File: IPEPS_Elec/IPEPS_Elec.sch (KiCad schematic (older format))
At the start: 26 parts

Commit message: secure AND unused inputs
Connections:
- wire segments 96 -> 100
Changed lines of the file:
@@
 	1    0    0    -1
 $EndComp
+$Comp
+L power:VCC #PWR?
+U 1 1 619B6EE2
+P 3735 4095
+F 0 "#PWR?" H 3735 3945 50  0001 C CNN
+F 1 "VCC" H 3750 4268 50  0000 C CNN
+F 2 "" H 3735 4095 50  0001 C CNN
+F 3 "" H 3735 4095 50  0001 C CNN
+	1    3735 4095
+	1    0    0    -1
+$EndComp
+$Comp
+L power:VCC #PWR?
+U 1 1 619B7C4D
+P 7340 1980
+F 0 "#PWR?" H 7340 1830 50  0001 C CNN
+F 1 "VCC" H 7355 2153 50  0000 C CNN
+F 2 "" H 7340 1980 50  0001 C CNN
+F 3 "" H 7340 1980 50  0001 C CNN
+	1    7340 1980
+	1    0    0    -1
+$EndComp
+Wire Wire Line
+	3735 4095 3735 4400
+Wire Wire Line
+	3735 4400 3860 4400
+Wire Wire Line
+	7340 1980 7340 2300
+Wire Wire Line
+	7340 2300 7440 2300
 $EndSCHEMATC

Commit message: wire the leds + add comments
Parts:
- removed D? (x3): LED, symbol Device:LED
- removed Q? (x3): BC547, Package_TO_SOT_THT:TO-92_Inline, symbol Transistor_BJT:BC547
- removed R? (x2): R_Small, symbol Device:R_Small
- added D?: T, symbol Device:LED
- added D?: L, symbol Device:LED
- added D?: RJ, symbol Device:LED
- added Q? (x3): BC547, Package_TO_SOT_THT:TO-92_Inline, symbol Transistor_BJT:BC547
- added R? (x3): 220R, symbol Device:R_Small
- added R? (x3): 47k, symbol Device:R_Small
- D?: value LED -> C; Colour (none) -> Green
- R?: value R_Small -> 220R
- R?: value R_Small -> 47k
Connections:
- net labels added: Out_C, Out_L, Out_RJ, Out_T
- wire segments 100 -> 108
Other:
- moved on the sheet: D?, Q?, R?

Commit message: simplify the XNOR
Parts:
- removed C?: 10uF, symbol Device:C_Small
- removed U?: SN74HC86N, digikey-footprints:DIP-14_W3mm, symbol IPEPS_Elec:SN74HC86N
- added U?: CD74HC7266E, Package_DIP:DIP-14_W7.62mm, symbol IPEPS_Elec:CD74HC7266E
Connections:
- wire segments 108 -> 99
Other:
- moved on the sheet: BAT?, Q?
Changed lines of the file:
@@
 L dk_Battery-Holders-Clips-Contacts:BS-7 BAT?
 U 1 1 61827D44
-P 1075 1625
-F 0 "BAT?" H 725 1700 60  0000 L CNN
-F 1 "BS-7" H 700 1600 60  0000 L CNN
-F 2 "digikey-footprints:Battery_Holder_Coin_2032_BS-7" H 1275 1825 60  0001 L CNN
-F 3 "http://www.memoryprotectiondevices.com/datasheets/BS-7-datasheet.pdf" V 1275 1925 60  0001 L CNN
-F 4 "BS-7-ND" H 1275 2025 60  0001 L CNN "Digi-Key_PN"
-F 5 "BS-7" H 1275 2125 60  0001 L CNN "MPN"
-F 6 "Battery Products" H 1275 2225 60  0001 L CNN "Category"
-F 7 "Battery Holders, Clips, Contacts" H 1275 2325 60  0001 L CNN "Family"
-F 8 "http://www.memoryprotectiondevices.com/datasheets/BS-7-datasheet.pdf" H 1275 2425 60  0001 L CNN "DK_Datasheet_Link"
-F 9 "/product-detail/en/mpd-memory-protection-devices/BS-7/BS-7-ND/389447" H 1275 2525 60  0001 L CNN "DK_Detail_Page"
-F 10 "BATTERY HOLDER COIN 20MM PC PIN" H 1275 2625 60  0001 L CNN "Description"
-F 11 "MPD (Memory Protection Devices)" H 1275 2725 60  0001 L CNN "Manufacturer"
-F 12 "Active" H 1275 2825 60  0001 L CNN "Status"
-	1    1075 1625
-	1    0    0    -1
-$EndComp
-Wire Wire Line
-	1750 1375 1075 1375
-Wire Wire Line
-	1075 1375 1075 1425
-Wire Wire Line
-	1075 1825 1950 1825
-Wire Wire Line
-	1950 1825 1950 1675
+P 945 1170
+F 0 "BAT?" H 595 1245 60  0000 L CNN
+F 1 "BS-7" H 570 1145 60  0000 L CNN
+F 2 "digikey-footprints:Battery_Holder_Coin_2032_BS-7" H 1145 1370 60  0001 L CNN
+F 3 "http://www.memoryprotectiondevices.com/datasheets/BS-7-datasheet.pdf" V 1145 1470 60  0001 L CNN
+F 4 "BS-7-ND" H 1145 1570 60  0001 L CNN "Digi-Key_PN"
+F 5 "BS-7" H 1145 1670 60  0001 L CNN "MPN"
+F 6 "Battery Products" H 1145 1770 60  0001 L CNN "Category"
+F 7 "Battery Holders, Clips, Contacts" H 1145 1870 60  0001 L CNN "Family"
+F 8 "http://www.memoryprotectiondevices.com/datasheets/BS-7-datasheet.pdf" H 1145 1970 60  0001 L CNN "DK_Datasheet_Link"
+F 9 "/product-detail/en/mpd-memory-protection-devices/BS-7/BS-7-ND/389447" H 1145 2070 60  0001 L CNN "DK_Detail_Page"
+F 10 "BATTERY HOLDER COIN 20MM PC PIN" H 1145 2170 60  0001 L CNN "Description"
+F 11 "MPD (Memory Protection Devices)" H 1145 2270 60  0001 L CNN "Manufacturer"
+F 12 "Active" H 1145 2370 60  0001 L CNN "Status"
+	1    945  1170
+	1    0    0    -1
+$EndComp
+Wire Wire Line
+	1620 920  945  920
+Wire Wire Line
+	945  920  945  970
+Wire Wire Line
+	945  1370 1820 1370
+Wire Wire Line
+	1820 1370 1820 1220
 $Comp
 L power:GND #PWR?
 U 1 1 61830670
-P 1075 1875
-F 0 "#PWR?" H 1075 1625 50  0001 C CNN
-F 1 "GND" H 1080 1702 50  0000 C CNN
-F 2 "" H 1075 1875 50  0001 C CNN
-F 3 "" H 1075 1875 50  0001 C CNN
-	1    1075 1875
-	1    0    0    -1
-$EndComp
-Wire Wire Line
-	1075 1825 1075 1875
-Connection ~ 1075 1825
+P 945 1420
+F 0 "#PWR?" H 945 1170 50  0001 C CNN
+F 1 "GND" H 950 1247 50  0000 C CNN
+F 2 "" H 945 1420 50  0001 C CNN
+F 3 "" H 945 1420 50  0001 C CNN
+	1    945  1420
+	1    0    0    -1
+$EndComp
+Wire Wire Line
+	945  1370 945  1420
+Connection ~ 945  1370
 $Comp
 L IPEPS_Elec:SN74HC11N U?
@@
 L Transistor_FET:AO3401A Q?
 U 1 1 61893D18
-P 1950 1475
-F 0 "Q?" V 2292 1475 50  0000 C CNN
-F 1 "AO3401A" V 2201 1475 50  0000 C CNN
-F 2 "Package_TO_SOT_SMD:SOT-23" H 2150 1400 50  0001 L CIN
-F 3 "http://www.aosmd.com/pdfs/datasheet/AO3401A.pdf" H 1950 1475 50  0001 L CNN
-	1    1950 1475
+P 1820 1020
+F 0 "Q?" V 2162 1020 50  0000 C CNN
+F 1 "AO3401A" V 2071 1020 50  0000 C CNN
+F 2 "Package_TO_SOT_SMD:SOT-23" H 2020 945 50  0001 L CIN
+F 3 "http://www.aosmd.com/pdfs/datasheet/AO3401A.pdf" H 1820 1020 50  0001 L CNN
+	1    1820 1020
 	0    -1   -1   0
 $EndComp
@@
 L power:VCC #PWR?
 U 1 1 61896917
-P 2300 1300
-F 0 "#PWR?" H 2300 1150 50  0001 C CNN
-F 1 "VCC" H 2315 1473 50  0000 C CNN
-F 2 "" H 2300 1300 50  0001 C CNN
-F 3 "" H 2300 1300 50  0001 C CNN
-	1    2300 1300
+P 2170 845
+F 0 "#PWR?" H 2170 695 50  0001 C CNN
+F 1 "VCC" H 2185 1018 50  0000 C CNN
+F 2 "" H 2170 845 50  0001 C CNN
+F 3 "" H 2170 845 50  0001 C CNN
+	1    2170 845
 	1    0    0    -1
 $EndComp
@@
 $EndComp
 Wire Wire Line
-	2150 1375 2300 1375
-Wire Wire Line
-	2300 1375 2300 1300
+	2020 920  2170 920
+Wire Wire Line
+	2170 920  2170 845
 $Comp
 L power:VCC #PWR?
@@
 	1    0    0    -1
 $EndComp
-Connection ~ 7100 3560
-Wire Wire Line
-	7100 3560 7100 3715
-Wire Wire Line
-	6600 3560 7100 3560
-Wire Wire Line
-	7100 3560 7100 3485
-$Comp
-L power:VCC #PWR?
-U 1 1 618FABB9
-P 7100 3485
-F 0 "#PWR?" H 7100 3335 50  0001 C CNN
-F 1 "VCC" H 7115 3658 50  0000 C CNN
-F 2 "" H 7100 3485 50  0001 C CNN
-F 3 "" H 7100 3485 50  0001 C CNN
-	1    7100 3485
-	1    0    0    -1
-$EndComp
-$Comp
-L Device:C_Small C?
-U 1 1 618F83E8
-P 6600 3660
-F 0 "C?" H 6475 3760 50  0000 L CNN
-F 1 "10uF" H 6375 3585 50  0000 L CNN
-F 2 "" H 6600 3660 50  0001 C CNN
-F 3 "~" H 6600 3660 50  0001 C CNN
-	1    6600 3660
-	1    0    0    -1
-$EndComp
-$Comp
-L power:GND #PWR?
-U 1 1 618F8054
-P 6600 3760
-F 0 "#PWR?" H 6600 3510 50  0001 C CNN
-F 1 "GND" H 6605 3587 50  0001 C CNN
-F 2 "" H 6600 3760 50  0001 C CNN
-F 3 "" H 6600 3760 50  0001 C CNN
-	1    6600 3760
-	1    0    0    -1
-$EndComp
-$Comp
-L IPEPS_Elec:SN74HC86N U?
-U 1 1 618F3369
-P 7100 5035
-F 0 "U?" H 6825 6310 50  0000 C CNN
-F 1 "SN74HC86N" H 7475 3810 50  0000 C CNN
-F 2 "digikey-footprints:DIP-14_W3mm" H 7830 6325 50  0001 C CNN
-F 3 "https://www.ti.com/lit/ds/symlink/sn74hc86.pdf?ts=1635939524941&ref_url=https%253A%252F%252Fwww.google.com%252F" H 7100 5305 50  0001 C CNN
-	1    7100 5035
-	1    0    0    -1
-$EndComp
 Wire Wire Line
 	2545 4200 2545 5415
@@
 Wire Wire Line
 	6460 5565 6460 4335
-Wire Wire Line
-	6460 4335 6660 4335
 Connection ~ 2400 4300
-Wire Wire Line
-	3815 1565 3655 1565
-Wire Wire Line
-	3655 1565 3655 2425
-Wire Wire Line
-	3655 2425 6515 2425
-Wire Wire Line
-	6515 2425 6515 3250
-Wire Wire Line
-	6515 3250 7530 3250
-Wire Wire Line
-	7530 3250 7530 4235
-Wire Wire Line
-	4415 1565 5700 1565
-Wire Wire Line
-	5700 1565 5700 2100
-Wire Wire Line
-	5700 2100 7440 2100
 Wire Wire Line
 	7225 2265 7225 2200
@@
 Wire Wire Line
 	10215 6050 10250 6050
+$Comp
+L IPEPS_Elec:CD74HC7266E U?
+U 1 1 6192A273
+P 6970 4235
+F 0 "U?" H 6970 4560 50  0000 C CNN
+F 1 "CD74HC7266E" H 6970 4469 50  0000 C CNN
+F 2 "Package_DIP:DIP-14_W7.62mm" H 6960 3935 50  0001 C CNN
+F 3 "https://www.ti.com/lit/ds/symlink/cd74hc7266.pdf" H 6970 4235 50  0001 C CNN
+	1    6970 4235
+	1    0    0    -1
+$EndComp
+Wire Wire Line
+	6460 4335 6670 4335
+Wire Wire Line
+	7270 4240 7270 4235
+Wire Wire Line
+	7270 2100 7440 2100
+Connection ~ 7270 4235
+Wire Wire Line
+	7270 4235 7270 2100
 $EndSCHEMATC

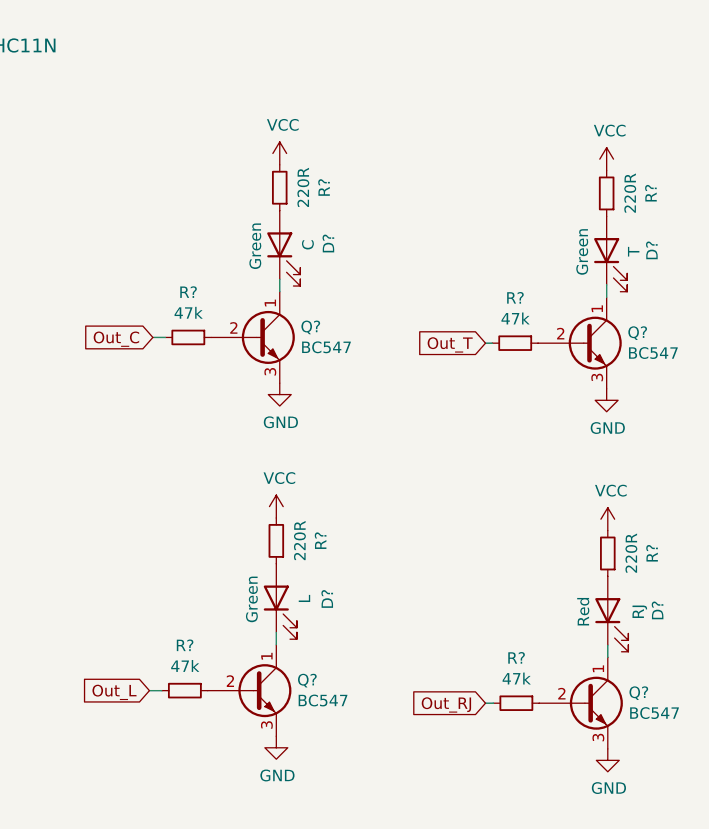
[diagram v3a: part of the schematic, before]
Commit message: change resistor values for 3V
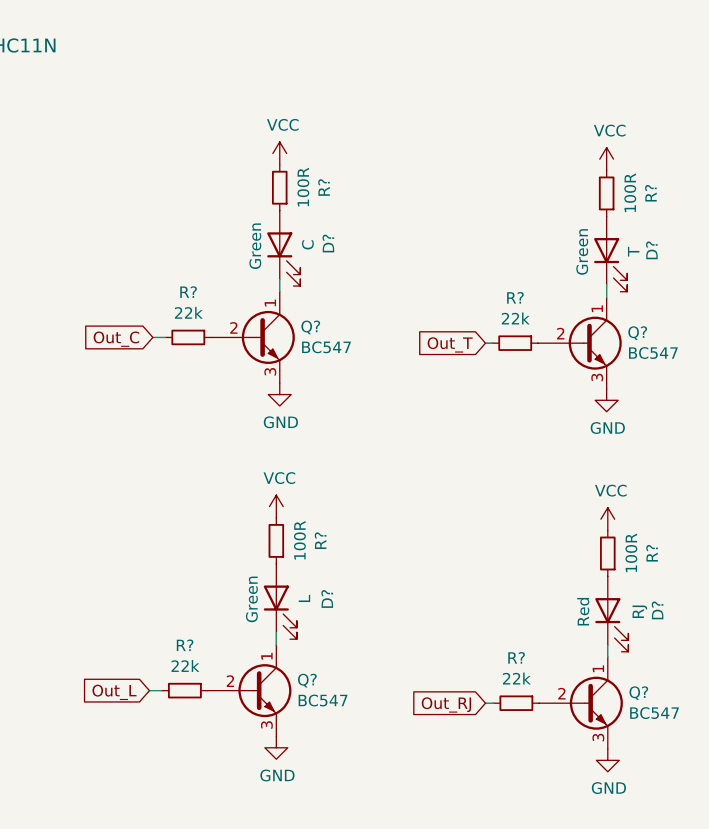
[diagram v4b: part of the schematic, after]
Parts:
- R? (x4): value 220R -> 100R
- R? (x4): value 47k -> 22k

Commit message: reorganise components
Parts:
- added R? (x4): 10k, symbol Device:R_Small
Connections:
- net GND: now also R?.1, R?.1, R?.1, R?.1
- net Out_C: now also U?.12 (1Y)
- net Out_L: now also U?.12 (1Y)
- net Out_RJ: now also U?.6 (2Y)
- net Out_T: now also U?.6 (2Y)
- net VCC: now also U?.3 (2A), U?.9 (3A); no longer U?.11 (3C), U?.5 (2C)
- net at U?.1 (1A): now also SW?.2, U?.1 (1A), U?.10 (3B), U?.2, R?.2; no longer U?.6 (3Y)
- net at U?.11 (3C): now also SW?.2, U?.1, U?.3 (2A), U?.3 (2A)
- net IN_J: now reaches SW?.2, U?.13 (1C), U?.13 (1C)
- net IN_J: now also U?.4 (2B), U?.5 (2C), R?.2; no longer U?.4 (2B), U?.5 (2C)
- net at U?.2 (1B): now also U?.4 (2Y); no longer SW?.2
- net at U?.3: now also U?.5 (2C); no longer U?.3 (2A)
- net C+T: now reaches U?.8 (3Y)
- net C+T: now also U?.5 (3A)
- net at U?.2 (1Y): now also U?.4 (2B); no longer U?.2 (1B)
- net at U?.8 (3Y): no longer U?.5 (3A)
- new net: R?.2, SW?.2, U?.1 (1A)
- new net: U?.2 (1B), U?.6 (3Y)
- now unconnected: U?.10 (3B), U?.9 (3A)
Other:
- moved on the sheet: BAT?, C?, D?, Q?, R?, SW?, U?, U?A

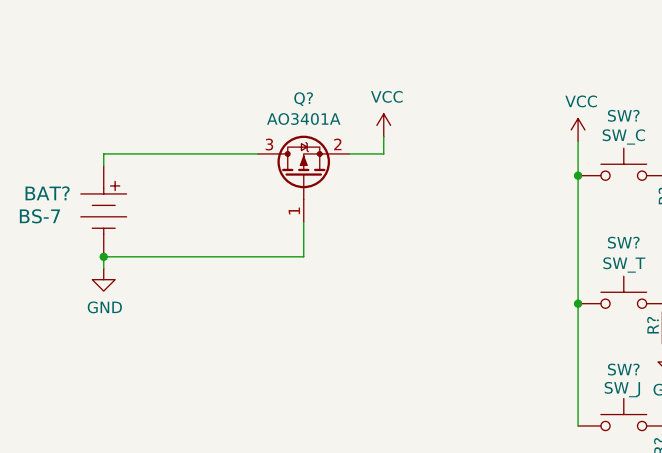
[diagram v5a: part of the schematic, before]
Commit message: add main switch
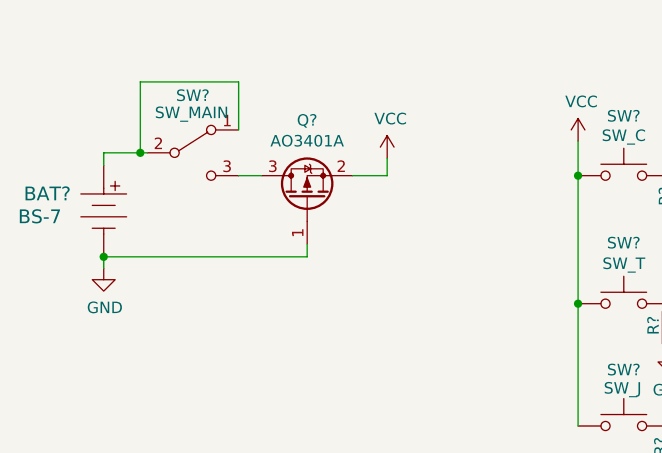
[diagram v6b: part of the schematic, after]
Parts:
- added SW?: SW_MAIN, symbol Switch:SW_SPDT
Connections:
- net at BAT?.Pos: now also SW?.1 (A), SW?.2 (B); no longer Q?.3 (D)
- new net: Q?.3 (D), SW?.3 (C)
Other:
- moved on the sheet: Q?
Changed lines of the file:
@@
 	1    0    0    -1
 $EndComp
-Wire Wire Line
-	1735 1205 1060 1205
-Wire Wire Line
-	1060 1205 1060 1255
-Wire Wire Line
-	1060 1655 1935 1655
-Wire Wire Line
-	1935 1655 1935 1505
 $Comp
 L power:GND #PWR?
@@
 L Transistor_FET:AO3401A Q?
 U 1 1 61893D18
-P 1935 1305
-F 0 "Q?" V 2277 1305 50  0000 C CNN
-F 1 "AO3401A" V 2186 1305 50  0000 C CNN
-F 2 "Package_TO_SOT_SMD:SOT-23" H 2135 1230 50  0001 L CIN
-F 3 "http://www.aosmd.com/pdfs/datasheet/AO3401A.pdf" H 1935 1305 50  0001 L CNN
-	1    1935 1305
+P 1950 1400
+F 0 "Q?" V 2292 1400 50  0000 C CNN
+F 1 "AO3401A" V 2201 1400 50  0000 C CNN
+F 2 "Package_TO_SOT_SMD:SOT-23" H 2150 1325 50  0001 L CIN
+F 3 "http://www.aosmd.com/pdfs/datasheet/AO3401A.pdf" H 1950 1400 50  0001 L CNN
+	1    1950 1400
 	0    -1   -1   0
 $EndComp
@@
 L power:VCC #PWR?
 U 1 1 61896917
-P 2285 1130
-F 0 "#PWR?" H 2285 980 50  0001 C CNN
-F 1 "VCC" H 2300 1303 50  0000 C CNN
-F 2 "" H 2285 1130 50  0001 C CNN
-F 3 "" H 2285 1130 50  0001 C CNN
-	1    2285 1130
+P 2300 1225
+F 0 "#PWR?" H 2300 1075 50  0001 C CNN
+F 1 "VCC" H 2315 1398 50  0000 C CNN
+F 2 "" H 2300 1225 50  0001 C CNN
+F 3 "" H 2300 1225 50  0001 C CNN
+	1    2300 1225
 	1    0    0    -1
 $EndComp
@@
 $EndComp
 Wire Wire Line
-	2135 1205 2285 1205
-Wire Wire Line
-	2285 1205 2285 1130
+	2150 1300 2300 1300
+Wire Wire Line
+	2300 1300 2300 1225
 $Comp
 L power:VCC #PWR?
@@
 Wire Wire Line
 	5220 5650 6230 5650
+$Comp
+L Switch:SW_SPDT SW?
+U 1 1 61B3D302
+P 1450 1200
+F 0 "SW?" H 1450 1450 50  0000 C CNN
+F 1 "SW_MAIN" H 1445 1375 50  0000 C CNN
+F 2 "" H 1450 1200 50  0001 C CNN
+F 3 "~" H 1450 1200 50  0001 C CNN
+	1    1450 1200
+	1    0    0    -1
+$EndComp
+Wire Wire Line
+	1950 1655 1950 1600
+Wire Wire Line
+	1060 1655 1950 1655
+Wire Wire Line
+	1650 1300 1750 1300
+Wire Wire Line
+	1060 1200 1220 1200
+Wire Wire Line
+	1060 1200 1060 1255
+Connection ~ 1220 1200
+Wire Wire Line
+	1220 1200 1250 1200
+Wire Wire Line
+	1650 890  1220 890
+Wire Wire Line
+	1650 890  1650 1100
+Wire Wire Line
+	1220 890  1220 1200
 $EndSCHEMATC

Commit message: add main decoupler
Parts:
- added C?: 10uF, symbol Device:CP1_Small
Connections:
- net GND: now also C?.2
- net VCC: now also C?.1
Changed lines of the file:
@@
 L power:VCC #PWR?
 U 1 1 61896917
-P 2300 1225
-F 0 "#PWR?" H 2300 1075 50  0001 C CNN
-F 1 "VCC" H 2315 1398 50  0000 C CNN
-F 2 "" H 2300 1225 50  0001 C CNN
-F 3 "" H 2300 1225 50  0001 C CNN
-	1    2300 1225
+P 2415 1230
+F 0 "#PWR?" H 2415 1080 50  0001 C CNN
+F 1 "VCC" H 2430 1403 50  0000 C CNN
+F 2 "" H 2415 1230 50  0001 C CNN
+F 3 "" H 2415 1230 50  0001 C CNN
+	1    2415 1230
 	1    0    0    -1
 $EndComp
@@
 	1    0    0    -1
 $EndComp
-Wire Wire Line
-	2150 1300 2300 1300
-Wire Wire Line
-	2300 1300 2300 1225
 $Comp
 L power:VCC #PWR?
@@
 Wire Wire Line
 	1220 890  1220 1200
+Wire Wire Line
+	2415 1300 2415 1230
+Wire Wire Line
+	2150 1300 2245 1300
+$Comp
+L Device:CP1_Small C?
+U 1 1 61B576AA
+P 2245 1440
+F 0 "C?" H 2336 1486 50  0000 L CNN
+F 1 "10uF" H 2336 1395 50  0000 L CNN
+F 2 "" H 2245 1440 50  0001 C CNN
+F 3 "~" H 2245 1440 50  0001 C CNN
+	1    2245 1440
+	1    0    0    -1
+$EndComp
+Wire Wire Line
+	2245 1340 2245 1300
+Connection ~ 2245 1300
+Wire Wire Line
+	2245 1300 2415 1300
+$Comp
+L power:GND #PWR?
+U 1 1 61B5BC87
+P 2245 1540
+F 0 "#PWR?" H 2245 1290 50  0001 C CNN
+F 1 "GND" H 2250 1367 50  0000 C CNN
+F 2 "" H 2245 1540 50  0001 C CNN
+F 3 "" H 2245 1540 50  0001 C CNN
+	1    2245 1540
+	1    0    0    -1
+$EndComp
 $EndSCHEMATC

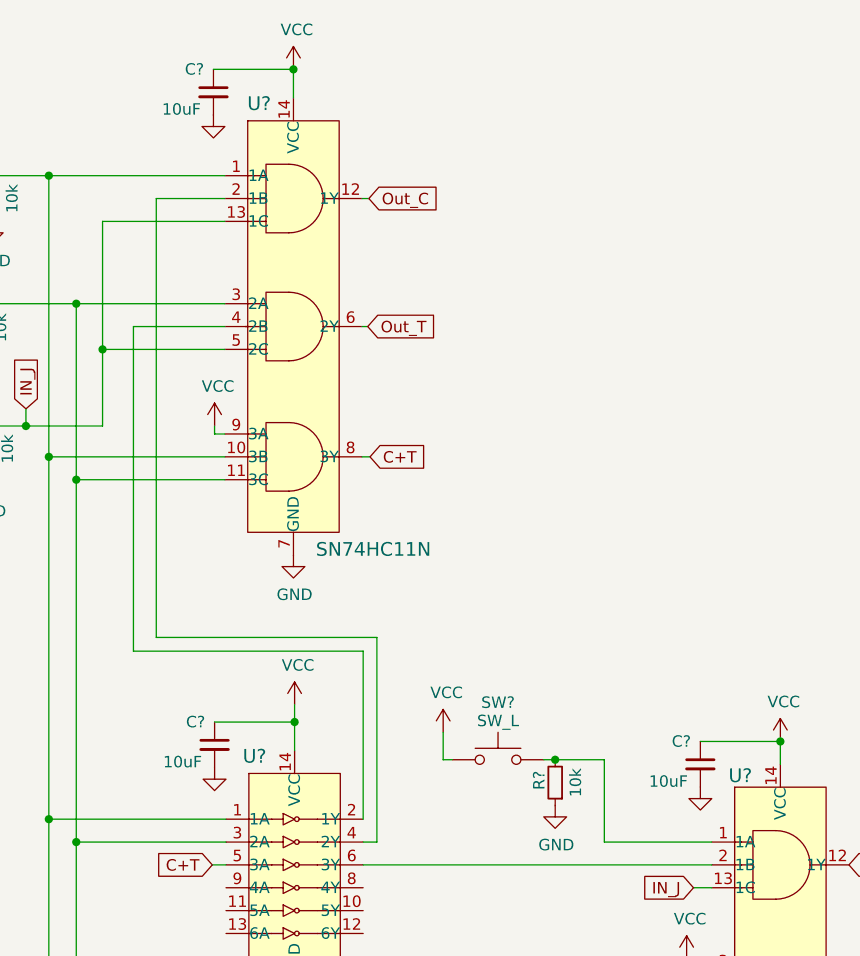
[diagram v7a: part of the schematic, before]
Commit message: change decouplers values
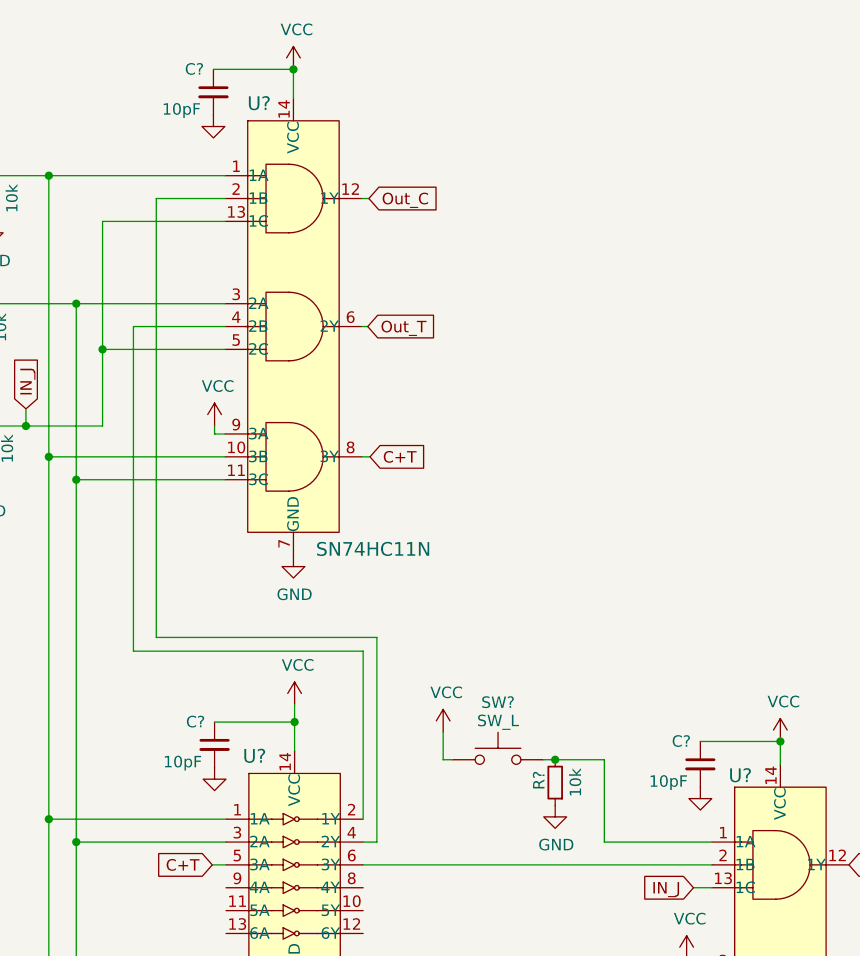
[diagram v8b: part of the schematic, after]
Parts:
- C? (x3): value 10uF -> 10pF
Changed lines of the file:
@@
 P 4560 3790
 F 0 "C?" H 4435 3890 50  0000 L CNN
-F 1 "10uF" H 4335 3715 50  0000 L CNN
+F 1 "10pF" H 4335 3715 50  0000 L CNN
 F 2 "" H 4560 3790 50  0001 C CNN
 F 3 "~" H 4560 3790 50  0001 C CNN
@@
 P 4555 935
 F 0 "C?" H 4430 1035 50  0000 L CNN
-F 1 "10uF" H 4330 860 50  0000 L CNN
+F 1 "10pF" H 4330 860 50  0000 L CNN
 F 2 "" H 4555 935 50  0001 C CNN
 F 3 "~" H 4555 935 50  0001 C CNN
@@
 P 6685 3875
 F 0 "C?" H 6560 3975 50  0000 L CNN
-F 1 "10uF" H 6460 3800 50  0000 L CNN
+F 1 "10pF" H 6460 3800 50  0000 L CNN
 F 2 "" H 6685 3875 50  0001 C CNN
 F 3 "~" H 6685 3875 50  0001 C CNN
